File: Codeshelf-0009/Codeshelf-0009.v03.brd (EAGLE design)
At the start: 26 parts, among them J1 CONTACT-SPRING-S7071-42R, J2 CONTACT-SPRING-S7071-42R, J3 CONTACT-SPRING-S7071-42R, J4 CONTACT-SPRING-S7071-42R, U1 MC9S08QG-DT, U2 LED5060A, U3 RS485SOIC, U4 CAT9552

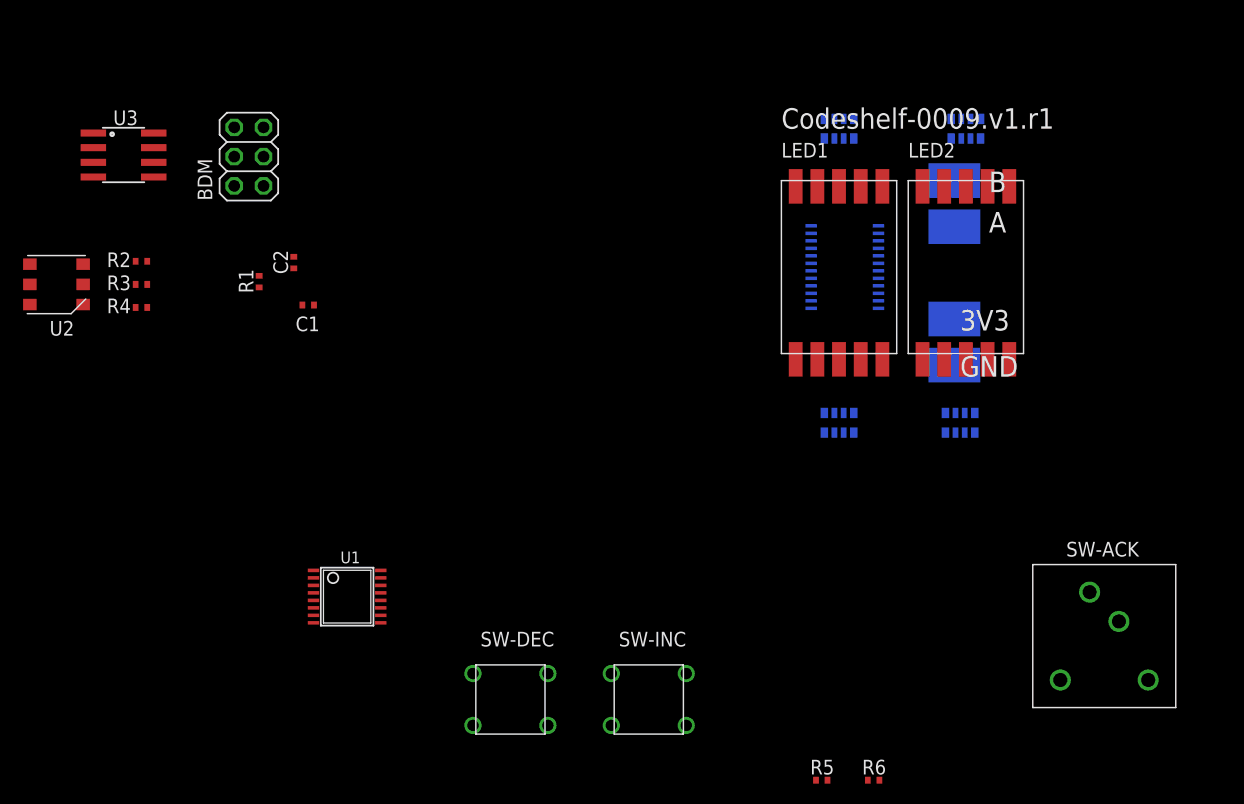
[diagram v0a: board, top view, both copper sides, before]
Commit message: KW2 and Slotflex edits
Removed RTC crystal from KW2, fixed (connected) switches in schematic of
0009.v02 and Slotflex v3 with RJ45 with NEW pinout (compatible with new
scanner pinout which doesn't exist yet in a CHE).
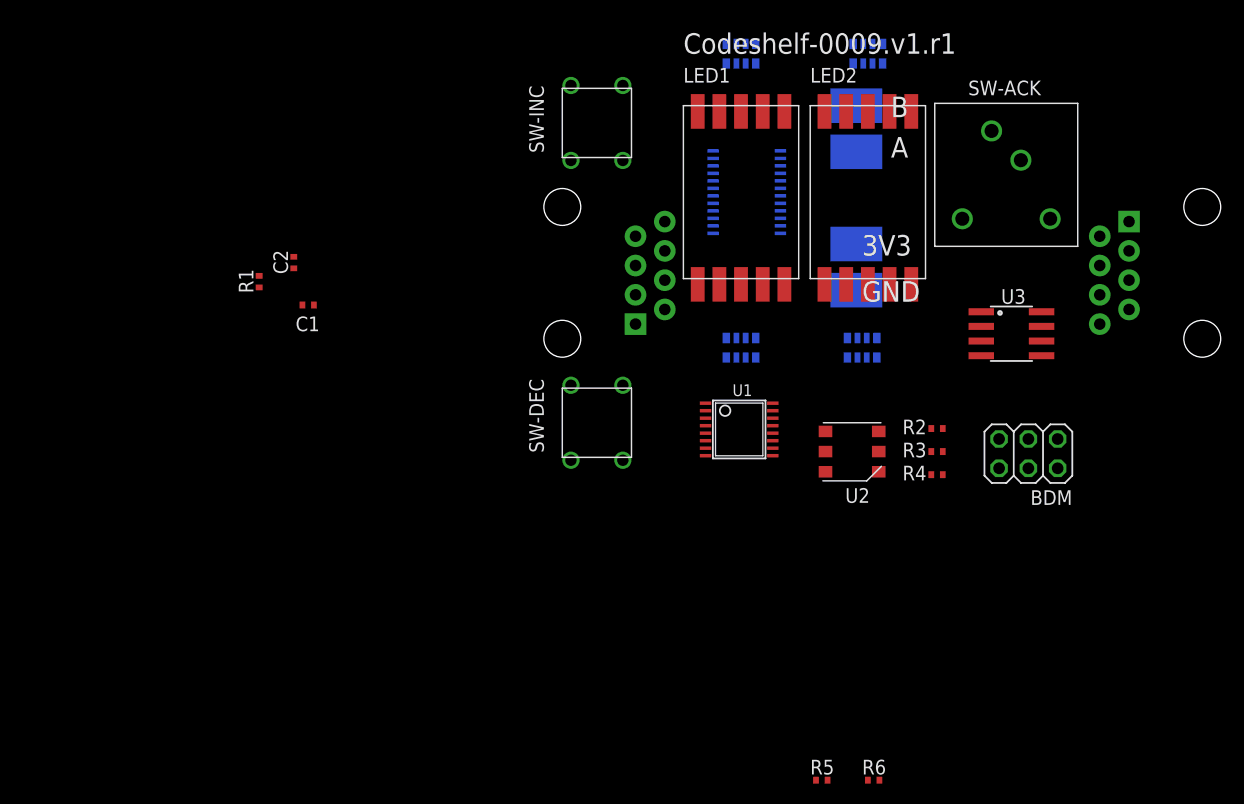
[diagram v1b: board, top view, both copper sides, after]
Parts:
- added U$1, U$2: RJ45-8PTH, GW-devices:RJ45-8
- moved U3 78.5 mm to (28.4, 6.72)
- moved R2 70.5 mm to (22.0, -1.50)
- moved R3 70.5 mm to (22.0, -3.50)
- moved R4 70.5 mm to (22.0, -5.50)
- moved U2 70.5 mm to (14.6, -3.50)
- moved BDM 69.3 mm to (27.4, -2.41), turned to 180 degrees
- moved SW-INC 50.2 mm to (-7.50, 25.0), turned to 90 degrees
- moved SW-ACK 40.9 mm to (28.0, 20.5)
- moved U1 37.0 mm to (4.84, -1.58)
- moved SW-DEC 25.1 mm to (-7.50, -1.00), turned to 90 degrees
- moved J1 10.7 mm to (15.0, 14.5)
- moved J2 10.7 mm to (15.0, 26.5)
- moved J3 10.7 mm to (15.0, 22.5)
- moved J4 10.7 mm to (15.0, 10.5)
- moved LED1 10.7 mm to (5.00, 18.5)
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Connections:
- net +3V3: now also U$1.1, U$1.8, U$2.1, U$2.8
- net A: now also U$1.5, U$2.5
- net B: now also U$1.4, U$2.4
- net GND: now also U$1.2, U$1.7, U$2.2, U$2.7

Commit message: Started new SlotFlex Layout
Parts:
- moved C2 79.8 mm to (44.8, -0.89), turned to 270 degrees
- moved R1 72.4 mm to (34.8, 0.26), turned to 270 degrees
- moved C1 65.5 mm to (32.6, 2.06), flipped to the bottom, turned to 270 degrees
- moved R5 58.5 mm to (-1.00, 25.0), flipped to the bottom, turned to 90 degrees
- moved R6 56.3 mm to (-1.00, 21.5), flipped to the bottom, turned to 90 degrees
- moved U1 23.2 mm to (27.8, 1.42), flipped to the bottom
- moved R4 19.0 mm to (5.00, 3.00), turned to 180 degrees
- moved R3 17.7 mm to (5.00, 1.50), turned to 180 degrees
- moved R2 17.1 mm to (5.00, 0.00), turned to 180 degrees
- moved U3 14.3 mm to (26.8, 20.9), turned to 0 degrees
- moved BDM 11.2 mm to (37.4, 2.59)
- moved SW-ACK 9.06 mm to (27.0, 11.5)
- moved R.D2D 8.60 mm to (20.5, 12.5), turned to 90 degrees
- moved R.D2B 7.90 mm to (5.00, 23.1)
- moved R.D2A 7.02 mm to (15.5, 24.0)
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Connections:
- net A renamed 485_P
- net B renamed 485_N
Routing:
- net 485_P: track 0.00 -> 71.0 mm
- net 485_N: track 0.00 -> 64.7 mm
- net GND: track 0.00 -> 38.9 mm
- net +3V3: track 0.00 -> 27.6 mm
- net N$7: track 0.00 -> 23.5 mm, vias 0 -> 1
- net N$24: track 0.00 -> 23.5 mm, vias 0 -> 1
- net N$38: track 0.00 -> 23.0 mm
- net N$37: track 0.00 -> 20.5 mm
- net N$23: track 0.00 -> 18.9 mm
- net N$36: track 0.00 -> 17.6 mm
- net N$5: track 0.00 -> 15.5 mm, vias 0 -> 1
- net N$35: track 0.00 -> 14.0 mm
- net N$6: track 0.00 -> 13.0 mm, vias 0 -> 1
- net N$22: track 0.00 -> 12.8 mm, vias 0 -> 1
- net N$9: track 0.00 -> 8.80 mm
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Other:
- board outline added: 71 x 30 mm

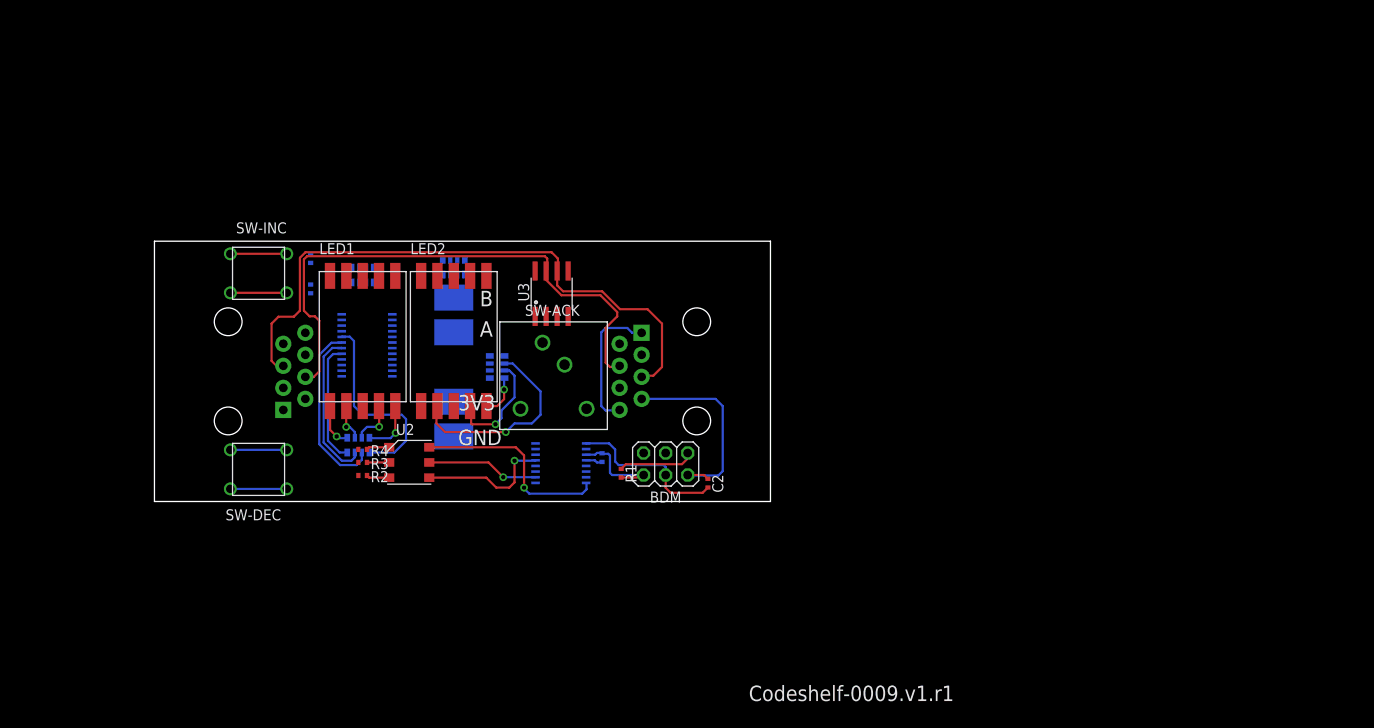
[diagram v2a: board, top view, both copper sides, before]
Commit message: Changed to SMD RJ45
Working on layout with new RJ45
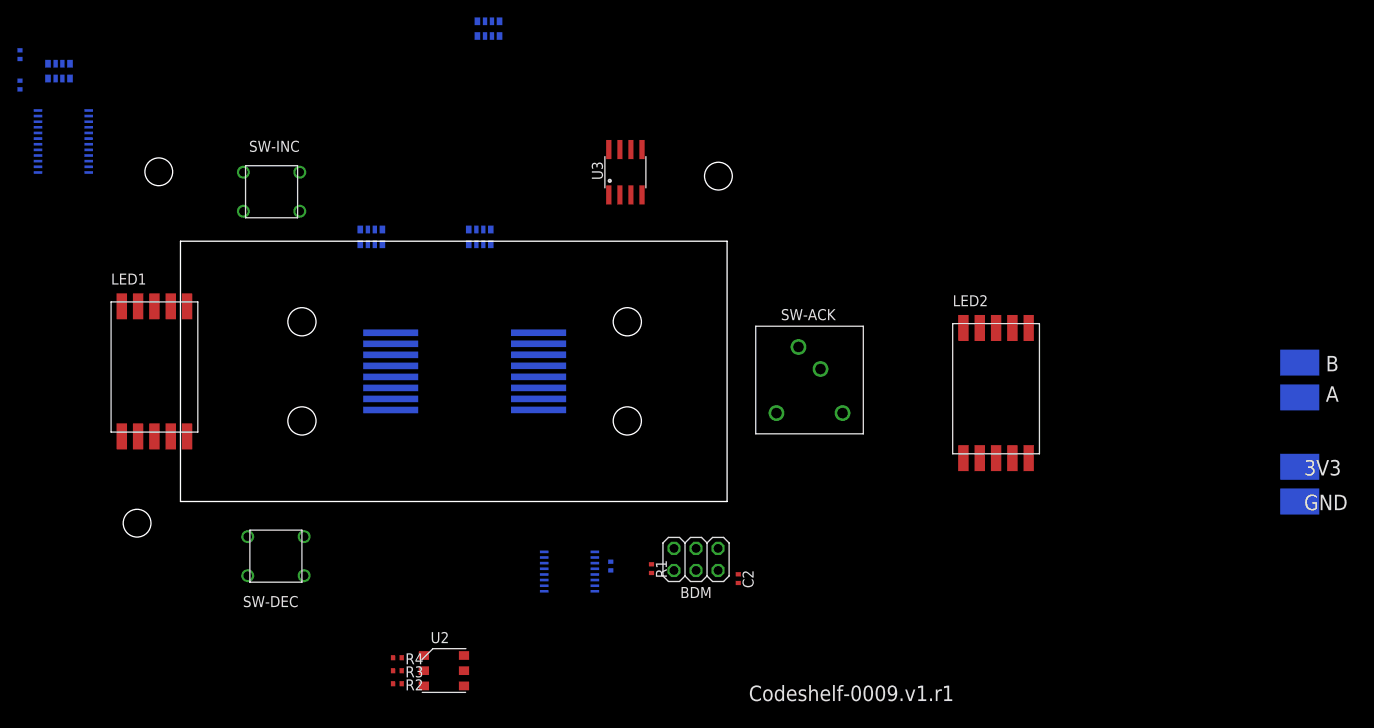
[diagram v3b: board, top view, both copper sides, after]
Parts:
- U$1, U$2: value RJ45-8PTH -> RJ45-8; device GW-devices:RJ45-8 -> GW-devices:MOLEX-0955016649
- moved J1 97.8 mm to (113.0, 1.00)
- moved J2 97.8 mm to (113.0, 13.0)
- moved J3 97.8 mm to (113.0, 9.00)
- moved J4 97.8 mm to (113.0, -3.00)
- moved LED2 62.8 mm to (78.0, 9.50)
- moved R.D2B 42.2 mm to (-30.0, 46.6)
- moved U4 42.2 mm to (-29.5, 38.5)
- moved R5 40.9 mm to (-34.5, 48.5)
- moved R6 40.9 mm to (-34.5, 45.0)
- moved SW-ACK 29.5 mm to (56.5, 11.0)
- moved R.D2A 27.8 mm to (19.5, 51.5)
- moved R2 24.3 mm to (9.00, -24.0)
- moved R3 24.3 mm to (9.00, -22.5)
- moved R4 24.3 mm to (9.00, -21.0)
- moved U2 24.3 mm to (14.4, -22.5)
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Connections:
- net +3V3: now also U$1.P$1, U$1.P$8, U$2.P$1, U$2.P$8; no longer U$1.1, U$1.8, U$2.1, U$2.8
- net 485_N: now also U$1.P$4, U$2.P$4; no longer U$1.4, U$2.4
- net 485_P: now also U$1.P$5, U$2.P$5; no longer U$1.5, U$2.5
- net GND: now also U$1.P$2, U$1.P$7, U$2.P$2, U$2.P$7; no longer U$1.2, U$1.7, U$2.2, U$2.7
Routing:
- net 485_P: track 71.0 -> 0.00 mm
- net 485_N: track 64.7 -> 0.00 mm
- net GND: track 38.9 -> 0.00 mm
- net +3V3: track 27.6 -> 0.00 mm
- net N$7: track 23.5 -> 0.00 mm, vias 1 -> 0
- net N$24: track 23.5 -> 0.00 mm, vias 1 -> 0
- net N$38: track 23.0 -> 0.00 mm
- net N$37: track 20.5 -> 0.00 mm
- net N$23: track 18.9 -> 0.00 mm
- net N$36: track 17.6 -> 0.00 mm
- net N$5: track 15.5 -> 0.00 mm, vias 1 -> 0
- net N$35: track 14.0 -> 0.00 mm
- net N$6: track 13.0 -> 0.00 mm, vias 1 -> 0
- net N$22: track 12.8 -> 0.00 mm, vias 1 -> 0
- net N$9: track 8.80 -> 0.00 mm
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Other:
- board size 71 x 30 mm -> 63 x 30 mm

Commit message: Position controller CAD models
Worked on exporting CAD models from Eagle for Marc. Chose form factor
for current version of small position controllers (NEMA enclosure lid)
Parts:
- removed SW-DEC, SW-INC: SWITCH-TACTILE-FSM, GW-devices:SWITCH-TACTILE-FSM
- added U$3, U$4: SWITCH-TACTILE, GW-devices:ESWITCH-TL3301PF
- moved U4 324.8 mm to (262.2, 181.2), flipped to the top, turned to 90 degrees
- moved R5 312.3 mm to (255.5, 164.4), flipped to the top, turned to 180 degrees
- moved R6 309.7 mm to (251.2, 164.4), flipped to the top, turned to 180 degrees
- moved LED1 300.6 mm to (229.8, 180.6)
- moved R.D2B 299.7 mm to (231.4, 193.2)
- moved R4 298.7 mm to (238.9, 169.6)
- moved R3 298.3 mm to (238.7, 167.8)
- moved R2 298.1 mm to (238.7, 166.1)
- moved U2 297.7 mm to (243.3, 167.8)
- moved BDM 291.2 mm to (250.8, 193.5)
- moved C1 289.7 mm to (261.8, 168.0)
- moved U$1 289.4 mm to (270.4, 181.0)
- moved U1 286.2 mm to (251.3, 169.0), flipped to the top, turned to 0 degrees
- moved U$2 279.7 mm to (220.8, 181.1)
- moved C2 277.5 mm to (259.7, 167.9), turned to 90 degrees
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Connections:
- net GND: now also U$3.3, U$3.4, U$4.3, U$4.4; no longer SW-DEC.P$3, SW-DEC.P$4, SW-INC.P$3, SW-INC.P$4
- net N$43: now also U$4.1, U$4.2; no longer SW-DEC.P$1, SW-DEC.P$2
- net N$45: now also U$3.1, U$3.2; no longer SW-INC.P$1, SW-INC.P$2
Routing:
- net N$11: track 0.00 -> 48.0 mm
- net N$10: track 0.00 -> 43.8 mm
- net N$8: track 0.00 -> 39.0 mm
- net N$2: track 0.00 -> 34.2 mm
- net N$20: track 0.00 -> 27.9 mm
- net N$18: track 0.00 -> 22.6 mm
- net N$17: track 0.00 -> 15.8 mm
- net N$29: track 0.00 -> 11.8 mm, vias 0 -> 1
- net N$28: track 0.00 -> 6.10 mm, vias 0 -> 1
- net N$16: track 0.00 -> 6.01 mm
- net N$26: track 0.00 -> 4.59 mm, vias 0 -> 1
- net N$27: track 0.00 -> 4.23 mm, vias 0 -> 1
- added copper zone on layer 1, net GND
- added copper zone on layer 16, net GND
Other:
- board size 63 x 30 mm -> 56.7 x 41.9 mm
- board text removed: "Codeshelf-0009.v1.r1"

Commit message: Targeting final PosController design
Moved everything to origin to make symmetric, screw hole locations and
partially complete layout. CAD models for this iteration.
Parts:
- moved U3 309.7 mm to (5.50, -16.7), turned to 270 degrees
- moved R.D2B 306.6 mm to (-16.0, 12.0)
- moved R.D2A 306.5 mm to (-3.90, 14.5)
- moved BDM 306.2 mm to (4.05, 12.1)
- moved U4 305.8 mm to (16.0, 0.00)
- moved R.D2D 305.7 mm to (-3.90, -14.5), flipped to the top, turned to 90 degrees
- moved U$1 305.4 mm to (24.4, 0.00)
- moved SW-ACK 305.3 mm to (5.45, 0.00)
- moved LED1 305.2 mm to (-16.1, 0.00)
- moved LED2 305.2 mm to (-5.95, 0.00)
- moved U$2 304.9 mm to (-24.4, 0.00)
- moved R.D2C 304.8 mm to (-16.0, -12.0)
- moved J1 304.6 mm to (-3.00, -4.00)
- moved J2 304.6 mm to (-3.00, 8.00)
- moved J3 304.6 mm to (-3.00, 4.00)
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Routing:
- net N$12: track 0.00 -> 55.4 mm, vias 0 -> 1
- net N$13: track 0.00 -> 54.6 mm, vias 0 -> 1
- net N$14: track 0.00 -> 52.6 mm, vias 0 -> 1
- net +3V3: track 0.00 -> 49.7 mm, vias 0 -> 1
- net N$15: track 0.00 -> 49.4 mm, vias 0 -> 1
- net N$35: track 0.00 -> 43.4 mm, vias 0 -> 1
- net N$36: track 0.00 -> 42.5 mm, vias 0 -> 1
- net N$37: track 0.00 -> 39.7 mm, vias 0 -> 1
- net N$38: track 0.00 -> 35.5 mm, vias 0 -> 1
- net N$32: track 0.00 -> 29.1 mm
- net N$31: track 0.00 -> 28.9 mm
- net N$33: track 0.00 -> 28.5 mm
- net N$34: track 0.00 -> 28.4 mm
- net N$25: track 0.00 -> 23.8 mm
- net N$24: track 0.00 -> 22.7 mm
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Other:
- board size 56.7 x 41.9 mm -> 55.8 x 40.9 mm
- board text removed: "3V3"
- board text removed: "A"
- board text removed: "B"
- board text removed: "GND"

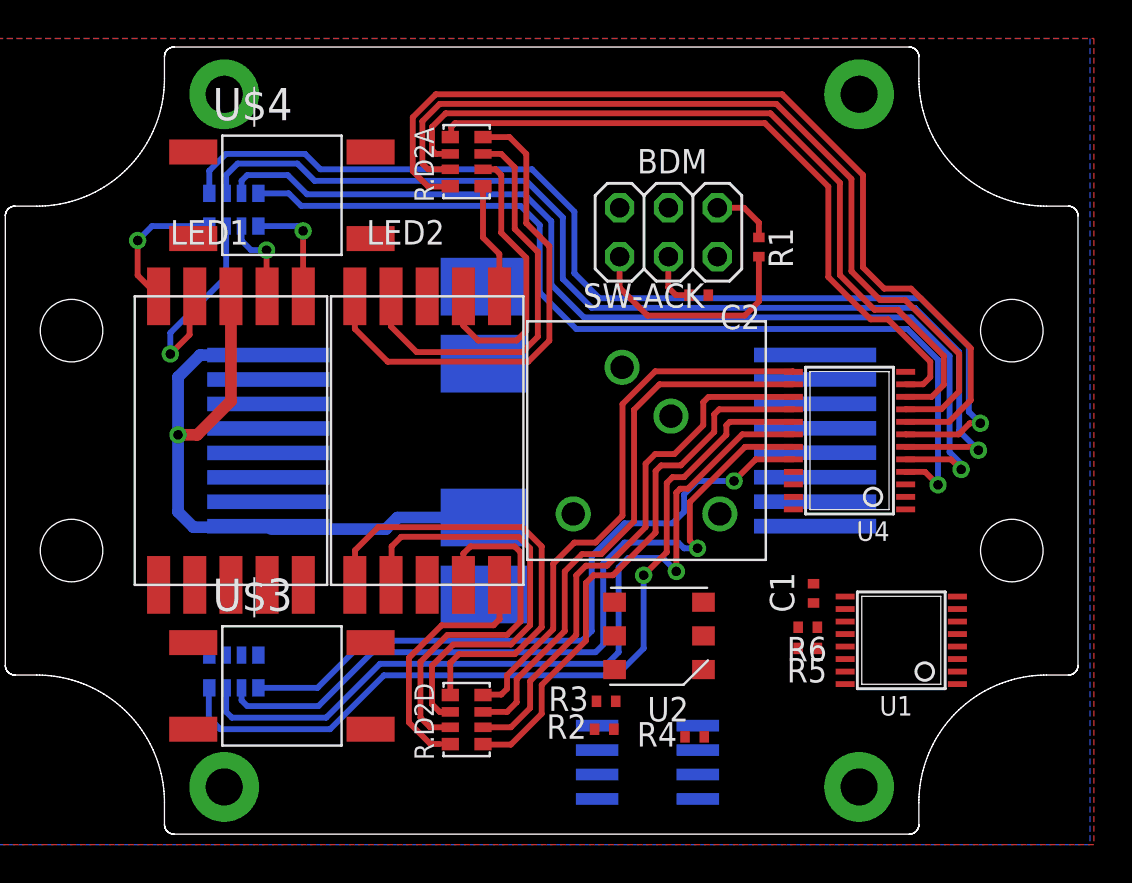
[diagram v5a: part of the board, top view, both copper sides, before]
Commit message: Finishing routing
Last few traces still incomplete.
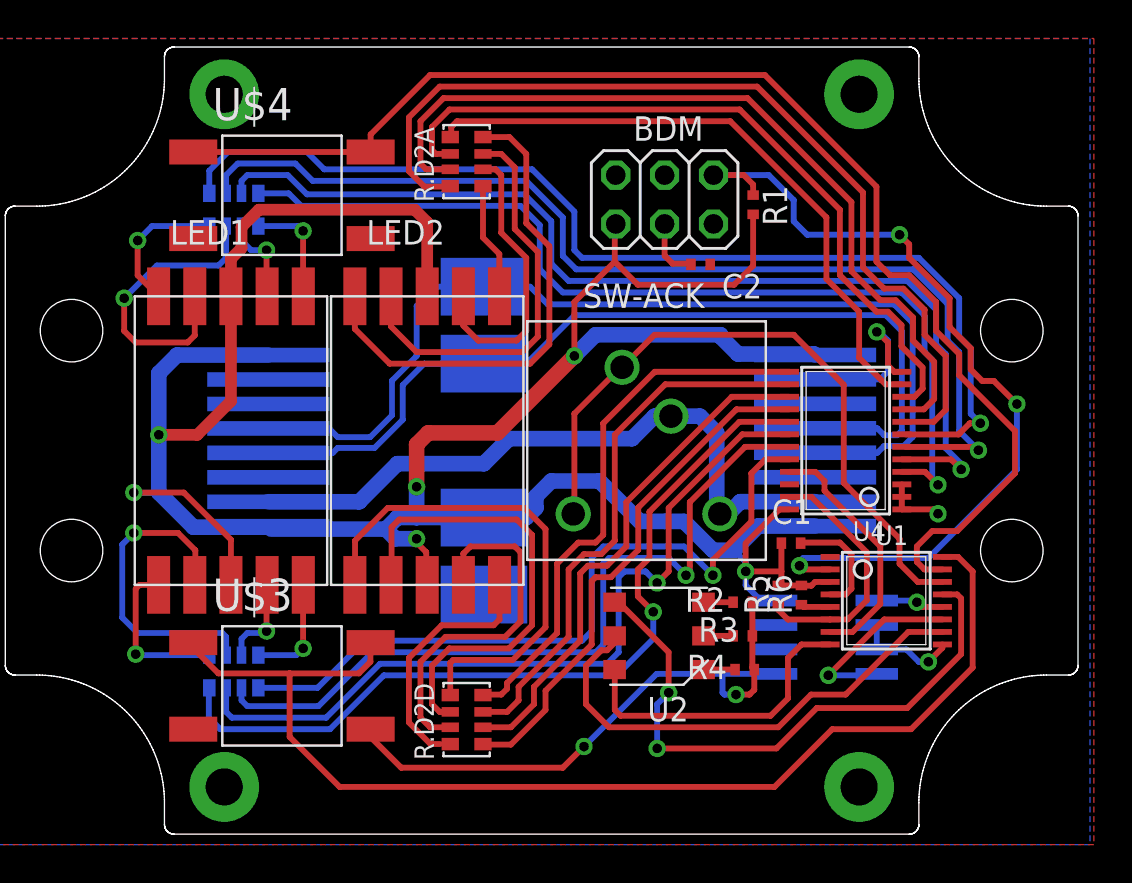
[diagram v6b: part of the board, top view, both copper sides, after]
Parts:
- moved U3 11.3 mm to (14.8, -10.2)
- moved R2 9.77 mm to (10.4, -8.40)
- moved R3 7.87 mm to (10.4, -10.2)
- moved R4 4.36 mm to (10.6, -11.9)
- moved J2 4.00 mm to (-3.00, 4.00), turned to 90 degrees
- moved J3 4.00 mm to (-3.00, 8.00)
- moved R5 3.16 mm to (12.3, -8.03), turned to 90 degrees
- moved C1 2.86 mm to (13.0, -5.33), turned to 0 degrees
- moved R1 2.22 mm to (11.0, 12.3)
- moved U1 2.20 mm to (17.9, -8.32), turned to 270 degrees
- moved BDM 1.71 mm to (3.85, 13.8)
- moved R6 1.70 mm to (13.5, -8.03), turned to 90 degrees
- moved C2 1.60 mm to (8.26, 9.16)
- moved U4 0.20 mm to (15.8, 0.00)
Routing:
- net +3V3: track 49.7 -> 154.1 mm, vias 1 -> 6
- net GND: track 0.00 -> 84.9 mm, vias 0 -> 4
- net N$43: track 0.00 -> 67.5 mm
- net N$45: track 0.00 -> 60.6 mm
- net 485_P: track 0.00 -> 51.6 mm
- net 485_N: track 0.00 -> 47.2 mm
- net N$9: track 3.25 -> 44.7 mm, vias 0 -> 3
- net N$42: track 0.00 -> 35.1 mm
- net N$5: track 0.00 -> 30.9 mm, vias 0 -> 2
- net N$6: track 0.00 -> 25.4 mm
- net N$40: track 0.00 -> 16.8 mm, vias 0 -> 1
- net N$7: track 0.00 -> 16.2 mm
- net SLA: track 0.00 -> 13.2 mm
- net RESET: track 0.00 -> 12.8 mm
- net TX: track 0.00 -> 9.68 mm, vias 0 -> 1
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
